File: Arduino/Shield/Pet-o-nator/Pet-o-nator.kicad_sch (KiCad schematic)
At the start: 9 parts, among them P1 Power, P2 Analog, P3 Digital, P4 Digital, P5 CONN_01X01, P6 CONN_01X01, P7 CONN_01X01, P8 CONN_01X01

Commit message: Correcting paths
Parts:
- removed DS?: (no value), symbol Display_Character:WC1602A
- added DS?: (no value), symbol Display_Character:WC1602A
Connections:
- net +5V: now also DS?.2 (VDD)
- net GND: now also DS?.1 (VSS)
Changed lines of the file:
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@@
     (pin "9")
   )
-  (symbol (lib_id "Display_Character:WC1602A") (at 110.49 107.95 0) (unit 1)
+  (symbol (lib_id "power:+5V") (at 129.54 64.77 0) (unit 1)
+    (in_bom yes) (on_board yes)
+    (property "Reference" "#PWR?" (id 0) (at 129.54 68.58 0)
+      (effects (font (size 1.27 1.27)) hide)
+    )
+    (property "Value" "+5V" (id 1) (at 129.54 59.69 90))
+    (property "Footprint" "" (id 2) (at 129.54 64.77 0))
+    (property "Datasheet" "" (id 3) (at 129.54 64.77 0))
+    (pin "1")
+  )
+  (symbol (lib_id "power:GND") (at 129.54 105.41 0) (unit 1)
+    (in_bom yes) (on_board yes)
+    (property "Reference" "#PWR?" (id 0) (at 129.54 111.76 0)
+      (effects (font (size 1.27 1.27)) hide)
+    )
+    (property "Value" "GND" (id 1) (at 129.54 109.22 0))
+    (property "Footprint" "" (id 2) (at 129.54 105.41 0))
+    (property "Datasheet" "" (id 3) (at 129.54 105.41 0))
+    (pin "1")
+  )
+  (symbol (lib_id "Display_Character:WC1602A") (at 129.54 85.09 0) (unit 1)
     (in_bom yes) (on_board yes) (fields_autoplaced)
-    (property "Reference" "DS?" (id 0) (at 112.5094 85.09 0)
+    (property "Reference" "DS?" (id 0) (at 131.5594 62.23 0)
       (effects (font (size 1.27 1.27)) (justify left))
     )
-    (property "Value" "" (id 1) (at 112.5094 87.63 0)
+    (property "Value" "" (id 1) (at 131.5594 64.77 0)
       (effects (font (size 1.27 1.27)) (justify left))
     )
-    (property "Footprint" "" (id 2) (at 110.49 130.81 0)
+    (property "Footprint" "" (id 2) (at 129.54 107.95 0)
       (effects (font (size 1.27 1.27) italic) hide)
     )
-    (property "Datasheet" "http://www.wincomlcd.com/pdf/WC1602A-SFYLYHTC06.pdf" (id 3) (at 128.27 107.95 0)
+    (property "Datasheet" "http://www.wincomlcd.com/pdf/WC1602A-SFYLYHTC06.pdf" (id 3) (at 147.32 85.09 0)
       (effects (font (size 1.27 1.27)) hide)
     )
@@
       (reference "#PWR04") (unit 1) (value "GND") (footprint "")
     )
-    (path "/5a0bbe49-66c1-45f6-bfcd-2960edb5ae37"
+    (path "/2d0cf03c-5b13-47a3-9764-aadc52cbfd49"
+      (reference "#PWR?") (unit 1) (value "+5V") (footprint "")
+    )
+    (path "/f2b44402-168e-4326-ae7a-f7682245d642"
+      (reference "#PWR?") (unit 1) (value "GND") (footprint "")
+    )
+    (path "/fa802958-3b80-4751-a02f-59eab1672067"
       (reference "DS?") (unit 1) (value "WC1602A") (footprint "Display:WC1602A")
     )

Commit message: New board
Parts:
- added C?: (no value), symbol Device:C
- added J1: (no value), symbol Connector:Conn_01x09_Male
- added Q?: (no value), symbol Transistor_FET:IRF540N
- added R1, R2, R4, R5: (no value), symbol Device:R
- added R3: (no value), Resistor_THT:R_Axial_DIN0309_L9.0mm_D3.2mm_P5.08mm_Vertical, symbol Device:R
- DS?: value (none) -> WC1602A; footprint (none) -> Display:WC1602A
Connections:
- net +5V: now also J1.5 (Pin_5), R1.1, R2.1
- net 7: now also R4.2
- net A0: now also C?.1, R5.1
- net GND: now also C?.2, J1.2 (Pin_2), J1.9 (Pin_9), R3.2
- new net +12V: J1.1 (Pin_1)
- new net IR Led: J1.7 (Pin_7), R1.2
- new net NTC Read: J1.6 (Pin_6), R3.1, R4.1, R5.2
- new net TIL78: J1.8 (Pin_8), R2.2
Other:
- note added: "Ground"
- note added: "Hot End (+)"
- note added: "Hot End (-)"
- note added: "IR LED (+)"
- note added: "IR Transistor (+)"
- note added: "IR counter"
- note added: "LED-Transistor (-)"
- note added: "Motor (+)"
- note added: "Motor (-)"
- note added: "NTC (+)"
- note added: "NTC (-)"
- note added: "NTC Reader"
- note added: "VCC 12V"
- moved on the sheet: DS?

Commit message: Retomada do desenvolvimento
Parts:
- added D? (x6): 1N4148, Diode_THT:D_DO-35_SOD27_P7.62mm_Horizontal, symbol Diode:1N4148
- added SW? (x9): SW_Push_DPDT, symbol Switch:SW_Push_DPDT
- C?: value (none) -> 100nF; footprint (none) -> Capacitor_THT:C_Rect_L7.2mm_W2.5mm_P5.00mm_FKS2_FKP2_MKS2_MKP2
- J1: value (none) -> Main_Plug; footprint (none) -> Connector_Phoenix_MSTB:PhoenixContact_MSTBVA_2,5_9-G_1x09_P5.00mm_Vertical
- Q?: value (none) -> IRF540N; footprint (none) -> Package_TO_SOT_THT:TO-220-3_Vertical
- R1: value (none) -> 220R; footprint (none) -> Resistor_THT:R_Axial_DIN0309_L9.0mm_D3.2mm_P5.08mm_Vertical
- R2: value (none) -> 220k; footprint (none) -> Resistor_THT:R_Axial_DIN0309_L9.0mm_D3.2mm_P5.08mm_Vertical
- R3: value (none) -> 10k
- R4: value (none) -> 520R; footprint (none) -> Resistor_THT:R_Axial_DIN0309_L9.0mm_D3.2mm_P5.08mm_Vertical
- R5: value (none) -> 10k; footprint (none) -> Resistor_THT:R_Axial_DIN0309_L9.0mm_D3.2mm_P5.08mm_Vertical
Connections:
- net 11(**/MOSI): now also D?.2 (A), D?.2 (A), SW?.3 (C), SW?.3 (C), SW?.6 (C), SW?.6 (C)
- net 12(MISO): now also D?.2 (A), D?.2 (A), SW?.3 (C), SW?.3 (C), SW?.3 (C), SW?.6 (C), SW?.6 (C), SW?.6 (C)
- net 13(SCK): now also D?.2 (A), D?.2 (A), SW?.3 (C), SW?.3 (C), SW?.3 (C), SW?.6 (C), SW?.6 (C), SW?.6 (C)
- new net: D?.1 (K), D?.1 (K), SW?.2 (B), SW?.2 (B), SW?.2 (B), SW?.5 (B), SW?.5 (B), SW?.5 (B) (x3)
- new net: SW?.3 (C), SW?.6 (C)
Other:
- note added: "Keypad"
- moved on the sheet: DS?, J1, Q?, R1, R2

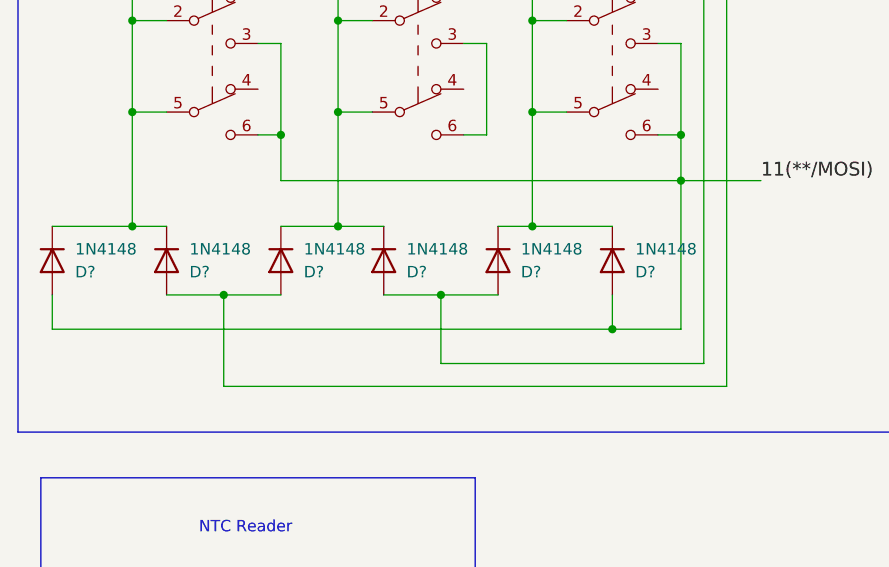
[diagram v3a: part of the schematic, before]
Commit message: New keyboard object ready
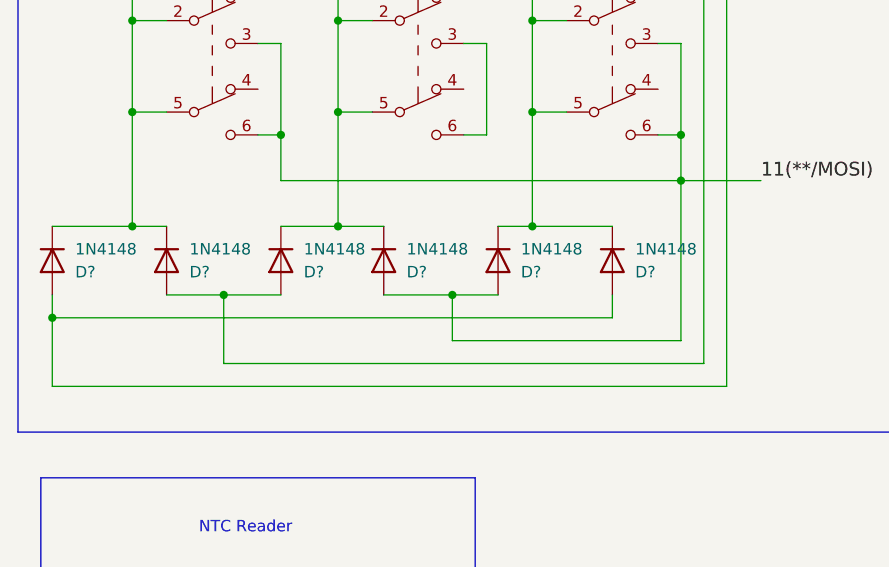
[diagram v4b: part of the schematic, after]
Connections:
- net 11(**/MOSI): now also D?.2 (A), D?.2 (A); no longer D?.2 (A), D?.2 (A)
- net 12(MISO): now also D?.2 (A), D?.2 (A); no longer D?.2 (A), D?.2 (A)
- net 13(SCK): now also D?.2 (A), D?.2 (A); no longer D?.2 (A), D?.2 (A)
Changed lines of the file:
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@@
   (junction (at 52.07 92.71) (diameter 0) (color 0 0 0 0)
   )
-  (junction (at 82.55 127) (diameter 0) (color 0 0 0 0)
+  (junction (at 64.77 123.19) (diameter 0) (color 0 0 0 0)
   )
   (junction (at 29.21 115.57) (diameter 0) (color 0 0 0 0)
@@
   (junction (at 45.72 105.41) (diameter 0) (color 0 0 0 0)
   )
-  (junction (at 63.5 123.19) (diameter 0) (color 0 0 0 0)
+  (junction (at 20.32 125.73) (diameter 0) (color 0 0 0 0)
   )
   (junction (at 90.17 53.34) (diameter 0) (color 0 0 0 0)
@@
     (stroke (width 0) (type default) (color 0 0 0 0))
   )
-  (wire (pts (xy 92.71 130.81) (xy 63.5 130.81))
+  (wire (pts (xy 39.37 130.81) (xy 92.71 130.81))
     (stroke (width 0) (type default) (color 0 0 0 0))
   )
@@
     (stroke (width 0) (type default) (color 0 0 0 0))
   )
-  (wire (pts (xy 39.37 123.19) (xy 45.72 123.19))
+  (wire (pts (xy 33.02 123.19) (xy 39.37 123.19))
     (stroke (width 0) (type default) (color 0 0 0 0))
   )
@@
     (stroke (width 0) (type default) (color 0 0 0 0))
   )
-  (wire (pts (xy 57.15 123.19) (xy 63.5 123.19))
+  (wire (pts (xy 57.15 123.19) (xy 64.77 123.19))
     (stroke (width 0) (type default) (color 0 0 0 0))
   )
@@
     (stroke (width 0) (type dash) (color 0 0 0 0))
   )
+  (wire (pts (xy 64.77 128.27) (xy 90.17 128.27))
+    (stroke (width 0) (type default) (color 0 0 0 0))
+  )
   (wire (pts (xy 40.64 166.37) (xy 43.18 166.37))
     (stroke (width 0) (type default) (color 0 0 0 0))
   )
-  (wire (pts (xy 39.37 133.35) (xy 39.37 123.19))
-    (stroke (width 0) (type default) (color 0 0 0 0))
-  )
   (wire (pts (xy 52.07 35.56) (xy 55.88 35.56))
     (stroke (width 0) (type default) (color 0 0 0 0))
@@
     (stroke (width 0) (type default) (color 0 0 0 0))
   )
-  (wire (pts (xy 90.17 127) (xy 82.55 127))
-    (stroke (width 0) (type default) (color 0 0 0 0))
-  )
   (polyline (pts (xy 257.81 163.83) (xy 232.41 163.83))
     (stroke (width 0) (type default) (color 0 0 0 0))
   )
+  (wire (pts (xy 39.37 123.19) (xy 45.72 123.19))
+    (stroke (width 0) (type default) (color 0 0 0 0))
+  )
   (wire (pts (xy 20.32 115.57) (xy 29.21 115.57))
     (stroke (width 0) (type default) (color 0 0 0 0))
@@
     (stroke (width 0) (type default) (color 0 0 0 0))
   )
+  (wire (pts (xy 64.77 123.19) (xy 64.77 128.27))
+    (stroke (width 0) (type default) (color 0 0 0 0))
+  )
   (wire (pts (xy 259.08 43.18) (xy 267.97 43.18))
     (stroke (width 0) (type solid) (color 0 0 0 0))
@@
     (stroke (width 0) (type default) (color 0 0 0 0))
   )
-  (wire (pts (xy 95.25 133.35) (xy 39.37 133.35))
+  (wire (pts (xy 95.25 133.35) (xy 20.32 133.35))
     (stroke (width 0) (type default) (color 0 0 0 0))
   )
@@
     (stroke (width 0) (type default) (color 0 0 0 0))
   )
-  (wire (pts (xy 20.32 123.19) (xy 20.32 127))
+  (wire (pts (xy 20.32 123.19) (xy 20.32 125.73))
     (stroke (width 0) (type default) (color 0 0 0 0))
   )
@@
     (stroke (width 0) (type default) (color 0 0 0 0))
   )
-  (wire (pts (xy 33.02 123.19) (xy 39.37 123.19))
-    (stroke (width 0) (type default) (color 0 0 0 0))
-  )
   (wire (pts (xy 29.21 35.56) (xy 33.02 35.56))
     (stroke (width 0) (type default) (color 0 0 0 0))
@@
   )
   (wire (pts (xy 90.17 53.34) (xy 95.25 53.34))
+    (stroke (width 0) (type default) (color 0 0 0 0))
+  )
+  (wire (pts (xy 20.32 125.73) (xy 82.55 125.73))
     (stroke (width 0) (type default) (color 0 0 0 0))
   )
@@
     (stroke (width 0) (type default) (color 0 0 0 0))
   )
-  (wire (pts (xy 90.17 110.49) (xy 90.17 127))
+  (wire (pts (xy 90.17 110.49) (xy 90.17 128.27))
     (stroke (width 0) (type default) (color 0 0 0 0))
   )
@@
     (stroke (width 0) (type solid) (color 0 0 0 0))
   )
-  (wire (pts (xy 20.32 127) (xy 82.55 127))
+  (wire (pts (xy 64.77 123.19) (xy 69.85 123.19))
     (stroke (width 0) (type default) (color 0 0 0 0))
   )
@@
     (stroke (width 0) (type dash) (color 0 0 0 0))
   )
+  (wire (pts (xy 20.32 125.73) (xy 20.32 133.35))
+    (stroke (width 0) (type default) (color 0 0 0 0))
+  )
   (wire (pts (xy 259.08 60.96) (xy 267.97 60.96))
     (stroke (width 0) (type solid) (color 0 0 0 0))
@@
   (wire (pts (xy 259.08 33.02) (xy 267.97 33.02))
     (stroke (width 0) (type solid) (color 0 0 0 0))
-  )
-  (wire (pts (xy 63.5 123.19) (xy 69.85 123.19))
-    (stroke (width 0) (type default) (color 0 0 0 0))
   )
   (wire (pts (xy 95.25 53.34) (xy 95.25 133.35))
@@
     (stroke (width 0) (type default) (color 0 0 0 0))
   )
+  (wire (pts (xy 39.37 130.81) (xy 39.37 123.19))
+    (stroke (width 0) (type default) (color 0 0 0 0))
+  )
   (wire (pts (xy 27.94 179.07) (xy 33.02 179.07))
     (stroke (width 0) (type default) (color 0 0 0 0))
@@
     (stroke (width 0) (type default) (color 0 0 0 0))
   )
-  (wire (pts (xy 82.55 127) (xy 82.55 123.19))
-    (stroke (width 0) (type default) (color 0 0 0 0))
-  )
-  (wire (pts (xy 63.5 130.81) (xy 63.5 123.19))
-    (stroke (width 0) (type default) (color 0 0 0 0))
-  )
+  (wire (pts (xy 82.55 125.73) (xy 82.55 123.19))
+    (stroke (width 0) (type default) (color 0 0 0 0))
+  )

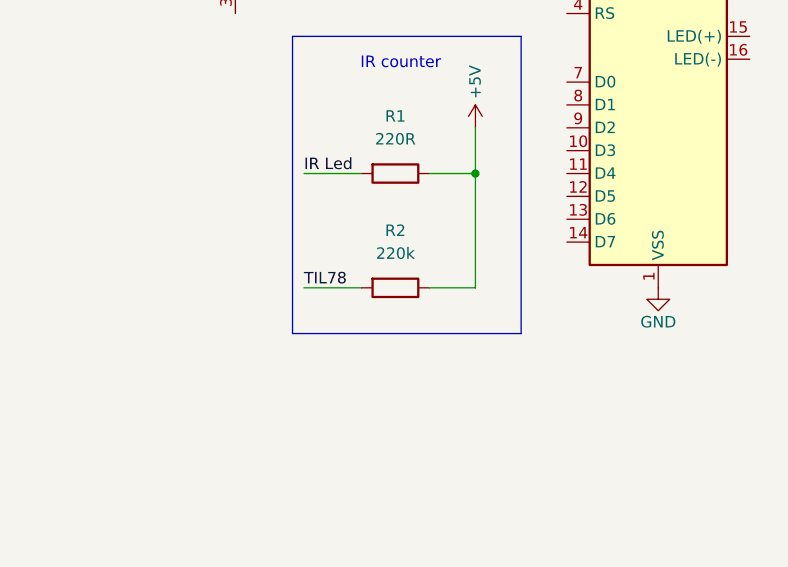
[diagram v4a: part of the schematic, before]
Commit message: Tachometer class giving results. Still debuging.
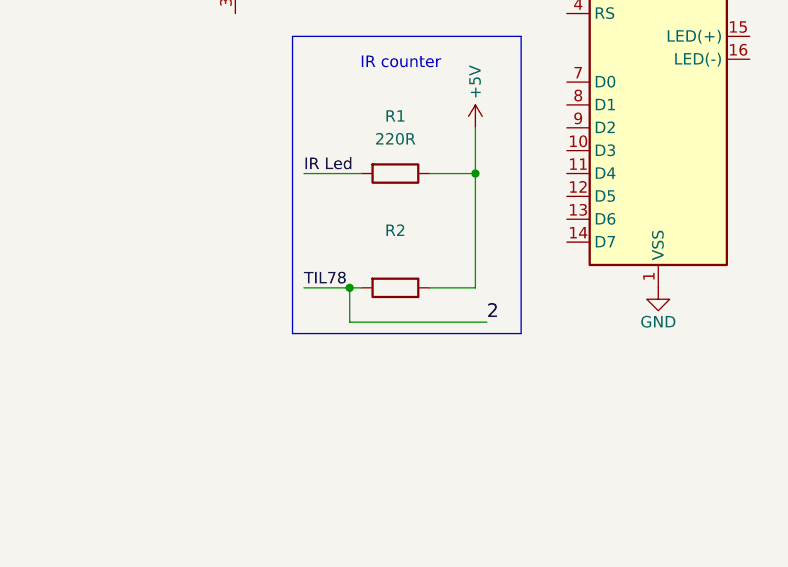
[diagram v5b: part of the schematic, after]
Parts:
- R2: value 220k -> (none); footprint Resistor_THT:R_Axial_DIN0309_L9.0mm_D3.2mm_P5.08mm_Vertical -> (none)
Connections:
- net TIL78 is gone; now on net 2: J1.8 (Pin_8), R2.2
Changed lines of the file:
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@@
   (junction (at 236.22 55.88) (diameter 1.016) (color 0 0 0 0)
+  )
+  (junction (at 238.76 158.75) (diameter 0) (color 0 0 0 0)
   )
   (junction (at 90.17 82.55) (diameter 0) (color 0 0 0 0)
@@
     (stroke (width 0) (type default) (color 0 0 0 0))
   )
-  (wire (pts (xy 233.68 158.75) (xy 240.03 158.75))
+  (wire (pts (xy 233.68 158.75) (xy 238.76 158.75))
     (stroke (width 0) (type default) (color 0 0 0 0))
   )
@@
     (stroke (width 0) (type default) (color 0 0 0 0))
   )
+  (wire (pts (xy 238.76 162.56) (xy 254 162.56))
+    (stroke (width 0) (type default) (color 0 0 0 0))
+  )
   (wire (pts (xy 259.08 43.18) (xy 267.97 43.18))
     (stroke (width 0) (type solid) (color 0 0 0 0))
@@
     (stroke (width 0) (type default) (color 0 0 0 0))
   )
+  (wire (pts (xy 238.76 158.75) (xy 238.76 162.56))
+    (stroke (width 0) (type default) (color 0 0 0 0))
+  )
   (wire (pts (xy 73.66 102.87) (xy 77.47 102.87))
     (stroke (width 0) (type default) (color 0 0 0 0))
@@
   )
   (wire (pts (xy 90.17 110.49) (xy 90.17 105.41))
+    (stroke (width 0) (type default) (color 0 0 0 0))
+  )
+  (wire (pts (xy 238.76 158.75) (xy 240.03 158.75))
     (stroke (width 0) (type default) (color 0 0 0 0))
   )
@@
   )
   (label "Vin" (at 227.33 36.83 90)
+    (effects (font (size 1.524 1.524)) (justify left bottom))
+  )
+  (label "2" (at 254 162.56 0)
     (effects (font (size 1.524 1.524)) (justify left bottom))
   )
@@
     (in_bom yes) (on_board yes) (fields_autoplaced)
     (property "Reference" "R2" (id 0) (at 243.84 152.4 90))
-    (property "Value" "220k" (id 1) (at 243.84 154.94 90))
-    (property "Footprint" "Resistor_THT:R_Axial_DIN0309_L9.0mm_D3.2mm_P5.08mm_Vertical" (id 2) (at 243.84 156.972 90)
-      (effects (font (size 1.27 1.27)) hide)
-    )
+    (property "Value" "" (id 1) (at 243.84 154.94 90))
+    (property "Footprint" "" (id 2) (at 243.84 156.972 90)
+      (effects (font (size 1.27 1.27)) hide)
+    )

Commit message: Updating schematics
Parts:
- added Q?: IRF540N, Package_TO_SOT_THT:TO-220-3_Vertical, symbol Transistor_FET:IRF540N
- added R3, R4, R5, R?: (no value), symbol Device:R
- added R?: 220R, Resistor_THT:R_Axial_DIN0309_L9.0mm_D3.2mm_P5.08mm_Vertical, symbol Device:R
- added U1: (no value), symbol Amplifier_Operational:LM324
- R2: value (none) -> 220k; footprint (none) -> Resistor_THT:R_Axial_DIN0309_L9.0mm_D3.2mm_P5.08mm_Vertical
- R6: renamed from R3; value 10k -> (none); footprint Resistor_THT:R_Axial_DIN0309_L9.0mm_D3.2mm_P5.08mm_Vertical -> (none)
- R8: renamed from R5; value 10k -> (none); footprint Resistor_THT:R_Axial_DIN0309_L9.0mm_D3.2mm_P5.08mm_Vertical -> (none)
- renumbered R4 to R7
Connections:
- net +5V: now also R4.1, U1.4 (V+)
- net 10(**/SS): now also R?.2
- net 2: now also R3.1, U1.1; no longer J1.8 (Pin_8), R2.2
- net 9(**): now also R?.2
- net GND: now also Q?.3 (S), Q?.3 (S), R5.2, U1.11 (V-)
- net Hot End: now reaches J1.3 (Pin_3)
- net Hot End: now also Q?.2 (D)
- net Motor: now reaches J1.4 (Pin_4)
- net Motor: now also Q?.2 (D)
- net at Q?.1 (G): now also R?.1
- new net: R3.2, R4.2, R5.1, U1.3 (+)
- new net: Q?.1 (G), R?.1
- new net TIL78: J1.8 (Pin_8), R2.2, U1.2 (-)
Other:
- moved on the sheet: Q?, R1, R2
